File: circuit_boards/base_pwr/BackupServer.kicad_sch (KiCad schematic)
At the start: 11 parts

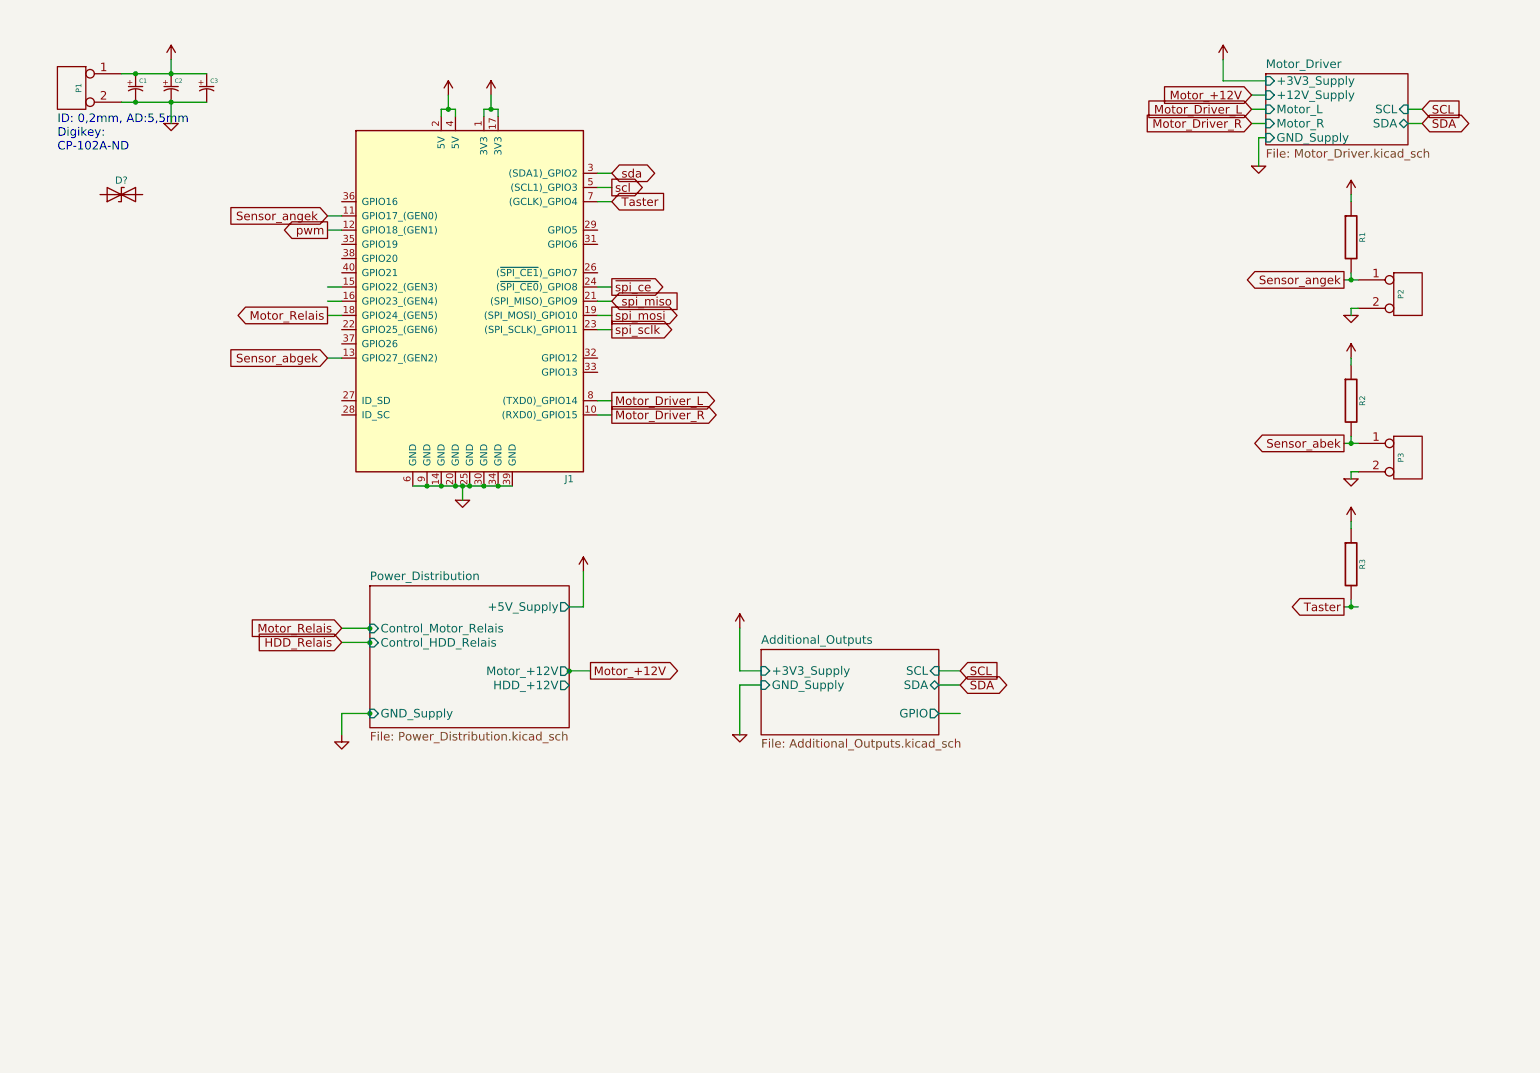
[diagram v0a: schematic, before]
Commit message: [HW] v2.0, made of the blue breadboard
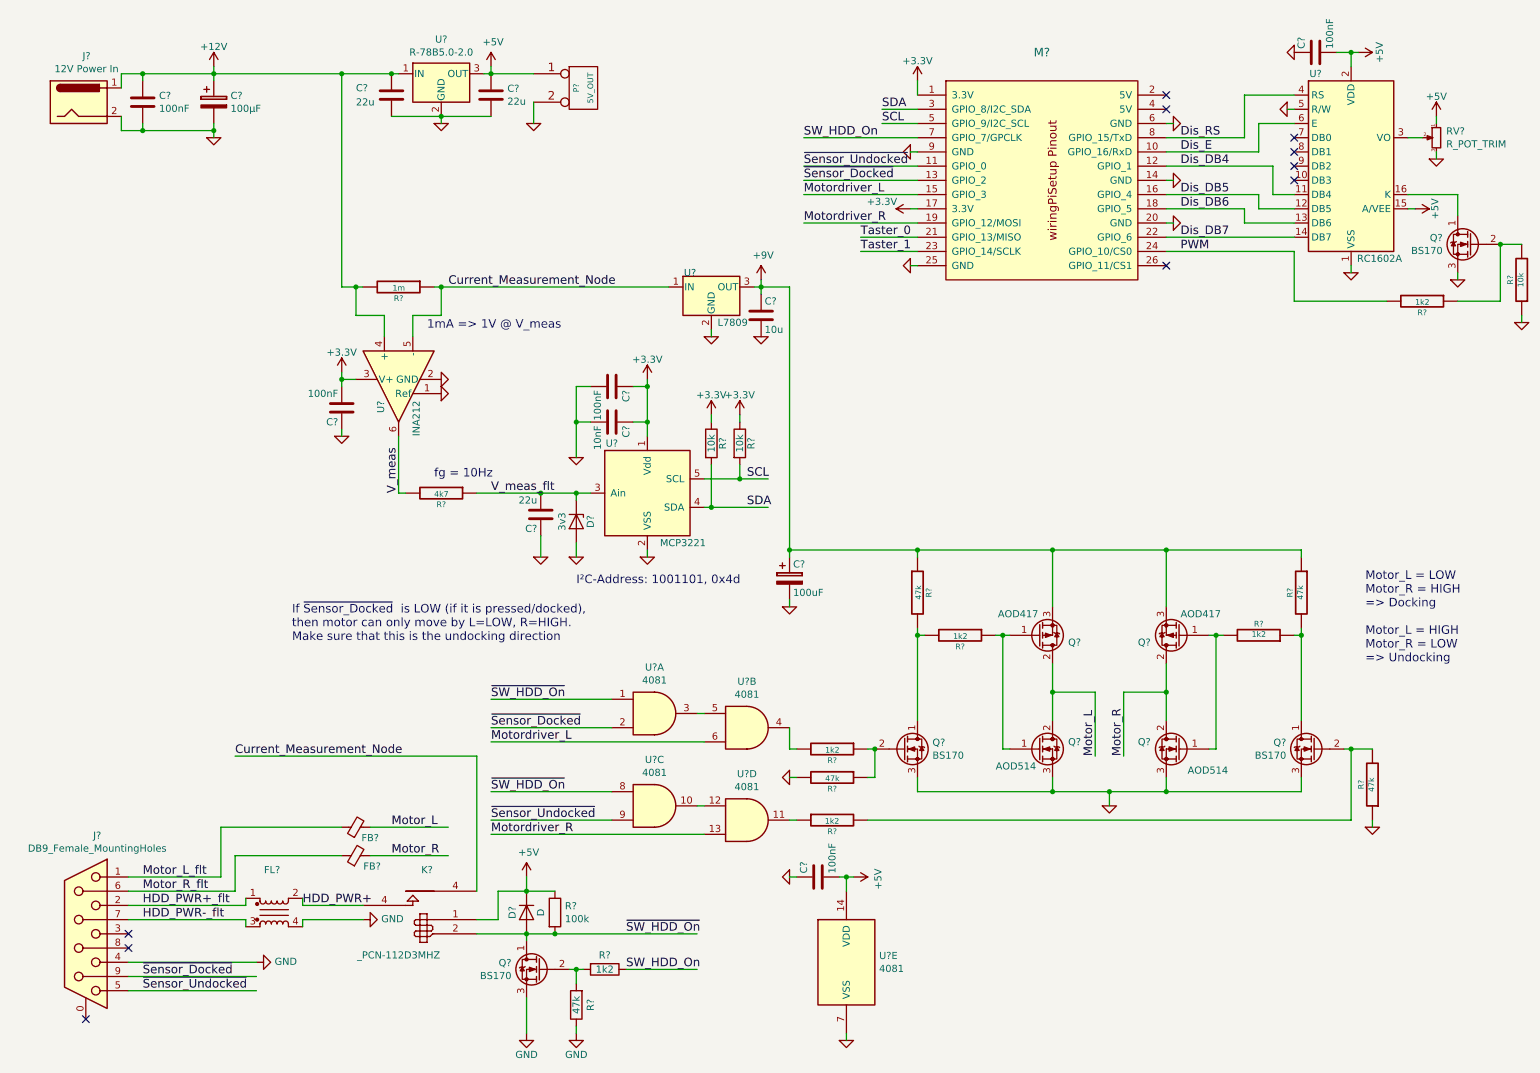
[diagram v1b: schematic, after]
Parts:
- removed C1, C2, C3: (no value), symbol BackupServer-rescue:CPsmall-
- removed D?: (no value), symbol BackupServer-rescue:D_TVS-
- removed J1: (no value), symbol BackupServer-rescue:Raspberry_Pi_2_3-
- removed P1, P2, P3: (no value), symbol BackupServer-rescue:CONN_2-
- removed R1, R2, R3: (no value), symbol BackupServer-rescue:R-RESCUE-BackupServer-
- added C? (x4): 100nF, Capacitors_SMD:C_0805_HandSoldering, symbol BackupServer-rescue:C-BackupServer-rescue
- added C?: 100nF, symbol BackupServer-rescue:C-BackupServer-rescue
- added C?: 100µF, symbol BackupServer-rescue:CP-BackupServer-rescue
- added C? (x2): 22u, symbol BackupServer-rescue:C-BackupServer-rescue
- added C?: 100uF, symbol BackupServer-rescue:CP-BackupServer-rescue
- added C?: 10nF, Capacitors_SMD:C_0805_HandSoldering, symbol BackupServer-rescue:C-BackupServer-rescue
- added C?: 10u, symbol BackupServer-rescue:C-BackupServer-rescue
- added C?: 22u, Capacitors_SMD:C_0805_HandSoldering, symbol BackupServer-rescue:C-BackupServer-rescue
- added D?: 3v3, symbol BackupServer-rescue:D_Zener-BackupServer-rescue
- added D?: D, symbol BackupServer-rescue:D-BackupServer-rescue
- added FB? (x2): (no value), symbol Device:FerriteBead_Small
- added FL?: (no value), symbol Device:Filter_EMI_CommonMode
- added J?: DB9_Female_MountingHoles, symbol Connector:DB9_Female_MountingHoles
- added J?: 12V Power In, symbol Connector:Barrel_Jack
- added K?: _PCN-112D3MHZ, symbol BackupServer-rescue:_PCN-112D3MHZ-BackupServer-rescue
- added M?: (no value), symbol g7_module_kicad6:BananaPi_M1-LeMaker
- added P?: 5V_OUT, Connect:BARREL_JACK, symbol BackupServer-rescue:CONN_2-BackupServer-rescue
- added Q? (x4): BS170, Package_TO_SOT_THT:TO-92_Inline, symbol Transistor_FET:BS170
- added Q? (x2): AOD514, TO_SOT_Packages_SMD:SOT-428, symbol BackupServer-rescue:Q_NMOS_GDS-BackupServer-rescue
- added Q? (x2): AOD417, TO_SOT_Packages_SMD:SOT-428, symbol BackupServer-rescue:Q_PMOS_GDS-BackupServer-rescue
- added R?: 1k2, symbol BackupServer-rescue:R-RESCUE-BackupServer-BackupServer-rescue
- added R? (x4): 1k2, Resistors_SMD:R_0805_HandSoldering, symbol BackupServer-rescue:R-RESCUE-BackupServer-BackupServer-rescue
- added R? (x2): 47k, Resistors_SMD:R_0805_HandSoldering, symbol BackupServer-rescue:R-RESCUE-BackupServer-BackupServer-rescue
- added R? (x2): 10k, Resistors_SMD:R_0805_HandSoldering, symbol BackupServer-rescue:R-BackupServer-rescue
- added R?: 1m, Resistors_SMD:R_2512_HandSoldering, symbol BackupServer-rescue:R-RESCUE-BackupServer-BackupServer-rescue
- added R?: 1k2, symbol BackupServer-rescue:R-BackupServer-rescue
- added R?: 4k7, Resistors_SMD:R_2512_HandSoldering, symbol BackupServer-rescue:R-RESCUE-BackupServer-BackupServer-rescue
- added R?: 47k, symbol BackupServer-rescue:R-BackupServer-rescue
- added R?: 10k, symbol BackupServer-rescue:R-RESCUE-BackupServer-BackupServer-rescue
- added R? (x2): 47k, symbol BackupServer-rescue:R-RESCUE-BackupServer-BackupServer-rescue
- added R?: 100k, symbol BackupServer-rescue:R-BackupServer-rescue
- added RV?: R_POT_TRIM, symbol Device:R_Potentiometer_Small
- added U?: R-78B5.0-2.0, Converter_DCDC:Converter_DCDC_RECOM_R-78B-2.0_THT, symbol Regulator_Switching:R-78B5.0-2.0
- added U?: MCP3221, symbol BackupServer-rescue:MCP3221-BackupServer-rescue
- added U?: INA212, TO_SOT_Packages_SMD:SC-70-6_Handsoldering, symbol BackupServer-rescue:INA212-BackupServer-rescue
- added U?: L7809, symbol Regulator_Linear:L7809
- added U? (x5): 4081, symbol 4xxx:4081
- added U?: RC1602A, Display:RC1602A, symbol Display_Character:RC1602A
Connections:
- net +12V: now also C?.1, C?.1, C?.1, J?.1, R?.2, U?.1 (IN), U?.4 (+)
- net +3V3: now also C?.1, C?.1, C?.2, M?.1 (3.3V), M?.17 (3.3V), R?.1, R?.1, U?.1 (Vdd), U?.3 (V+)
- net +5V: now also C?.1, C?.2, C?.2, D?.1 (K), K?.1, P?.1 (P1), R?.1, RV?.1, U?.14 (VDD), U?.15 (A/VEE), U?.2 (VDD), U?.3 (OUT)
- net GND: now also C?.1, C?.1, C?.1, C?.1, C?.2, C?.2, C?.2, C?.2, C?.2, C?.2, C?.2, C?.2, D?.2 (A), FL?.4, J?.2, J?.4, M?.14 (GND), M?.20 (GND), M?.25 (GND), M?.6 (GND), M?.9 (GND), P?.2 (PM), Q?.3 (S), Q?.3 (S), Q?.3 (S), Q?.3 (S), Q?.3 (S), Q?.3 (S), R?.1, R?.1, R?.1, R?.2, RV?.3, U?.1 (Ref), U?.1 (VSS), U?.2 (GND), U?.2 (GND), U?.2 (GND), U?.2 (VSS), U?.5 (R/W), U?.7 (VSS)
- net SCL: now also M?.5 (GPIO_9/I2C_SCL), R?.2, U?.5 (SCL)
- net SDA: now also M?.3 (GPIO_8/I2C_SDA), R?.2, U?.4 (SDA)
- new net: Q?.2 (G), R?.1, R?.2
- new net: RV?.2, U?.3 (VO)
- new net: Q?.1 (D), U?.16 (K)
- new net: Q?.1 (G), Q?.1 (G), R?.1
- new net: Q?.1 (D), R?.2, R?.2
- new net: Q?.1 (D), R?.1, R?.2
- new net: Q?.1 (G), Q?.1 (G), R?.2
- new net: R?.1, U?.11
- new net: Q?.2 (G), R?.2, R?.2 (x2)
- new net: Q?.2 (G), R?.1, R?.1
- new net: R?.2, U?.4
- new net: U?.3, U?.5
- new net: U?.10, U?.12
- new net +9V: C?.1, C?.1, Q?.3 (S), Q?.3 (S), R?.1, R?.1, U?.3 (OUT)
- new net Current_Measurement_Node: K?.4, R?.1, U?.1 (IN), U?.5 (-)
- new net Dis_DB4: M?.12 (GPIO_1), U?.11 (DB4)
- new net Dis_DB5: M?.16 (GPIO_4), U?.12 (DB5)
- new net Dis_DB6: M?.18 (GPIO_5), U?.13 (DB6)
- new net Dis_DB7: M?.22 (GPIO_6), U?.14 (DB7)
- new net Dis_E: M?.10 (GPIO_16/RxD), U?.6 (E)
- new net Dis_RS: M?.8 (GPIO_15/TxD), U?.4 (RS)
- new net HDD_PWR+: FL?.2, K?.4
- new net HDD_PWR+_flt: FL?.1, J?.2
- new net HDD_PWR-_flt: FL?.3, J?.7
- new net Motor_L: FB?.2, Q?.2 (D), Q?.2 (D)
- new net Motor_L_flt: FB?.1, J?.1
- new net Motor_R: FB?.2, Q?.2 (D), Q?.2 (D)
- new net Motor_R_flt: FB?.1, J?.6
- new net Motordriver_L: M?.15 (GPIO_3), U?.6
- new net Motordriver_R: M?.19 (GPIO_12/MOSI), U?.13
- new net PWM: M?.24 (GPIO_10/CS0), R?.2
- new net SW_HDD_On: M?.7 (GPIO_7/GPCLK), R?.1
- new net Taster_0: M?.21 (GPIO_13/MISO)
- new net Taster_1: M?.23 (GPIO_14/SCLK)
- new net V_meas: R?.2, U?.6
- new net V_meas_flt: C?.2, D?.1 (K), R?.1, U?.3 (Ain)
- new net ~{SW_HDD_On}: D?.2 (A), K?.2, Q?.1 (D), R?.2, U?.1, U?.8
- new net ~{Sensor_Docked}: J?.9, M?.13 (GPIO_2), U?.2
- new net ~{Sensor_Undocked}: J?.5, M?.11 (GPIO_0), U?.9
- no-connect marks 0 -> 10
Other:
- removed sheet Additional_Outputs
- removed sheet Motor_Driver
- removed sheet Power_Distribution
- note added: "1mA => 1V @ V_meas"
- note added: "If ~{Sensor_Docked} is LOW (if it is pressed/docked), then motor can only move by L=LOW, R=HIGH. Make sure that this is the undocking direction"
- note added: "I²C-Address: 1001101, 0x4d"
- note added: "Motor_L = LOW Motor_R = HIGH => Docking Motor_L = HIGH Motor_R = LOW => Undocking"
- note added: "fg = 10Hz"
- note removed: "ID: 0,2mm, AD:5,5mm Digikey: CP-102A-ND"
- company: always on the run ... -> Gras7 Labs
